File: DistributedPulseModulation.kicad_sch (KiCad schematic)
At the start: 59 parts, among them J1 Conn_02x12_Odd_Even, J2 Conn_01x01, U1 74LS251, U10 4053, U11 4053, U12 4053, U25 74LS85, U28 74LS85, U31 74LS85, U4 MCP23017_SP, U7 4053, U8 4040, U9 4040

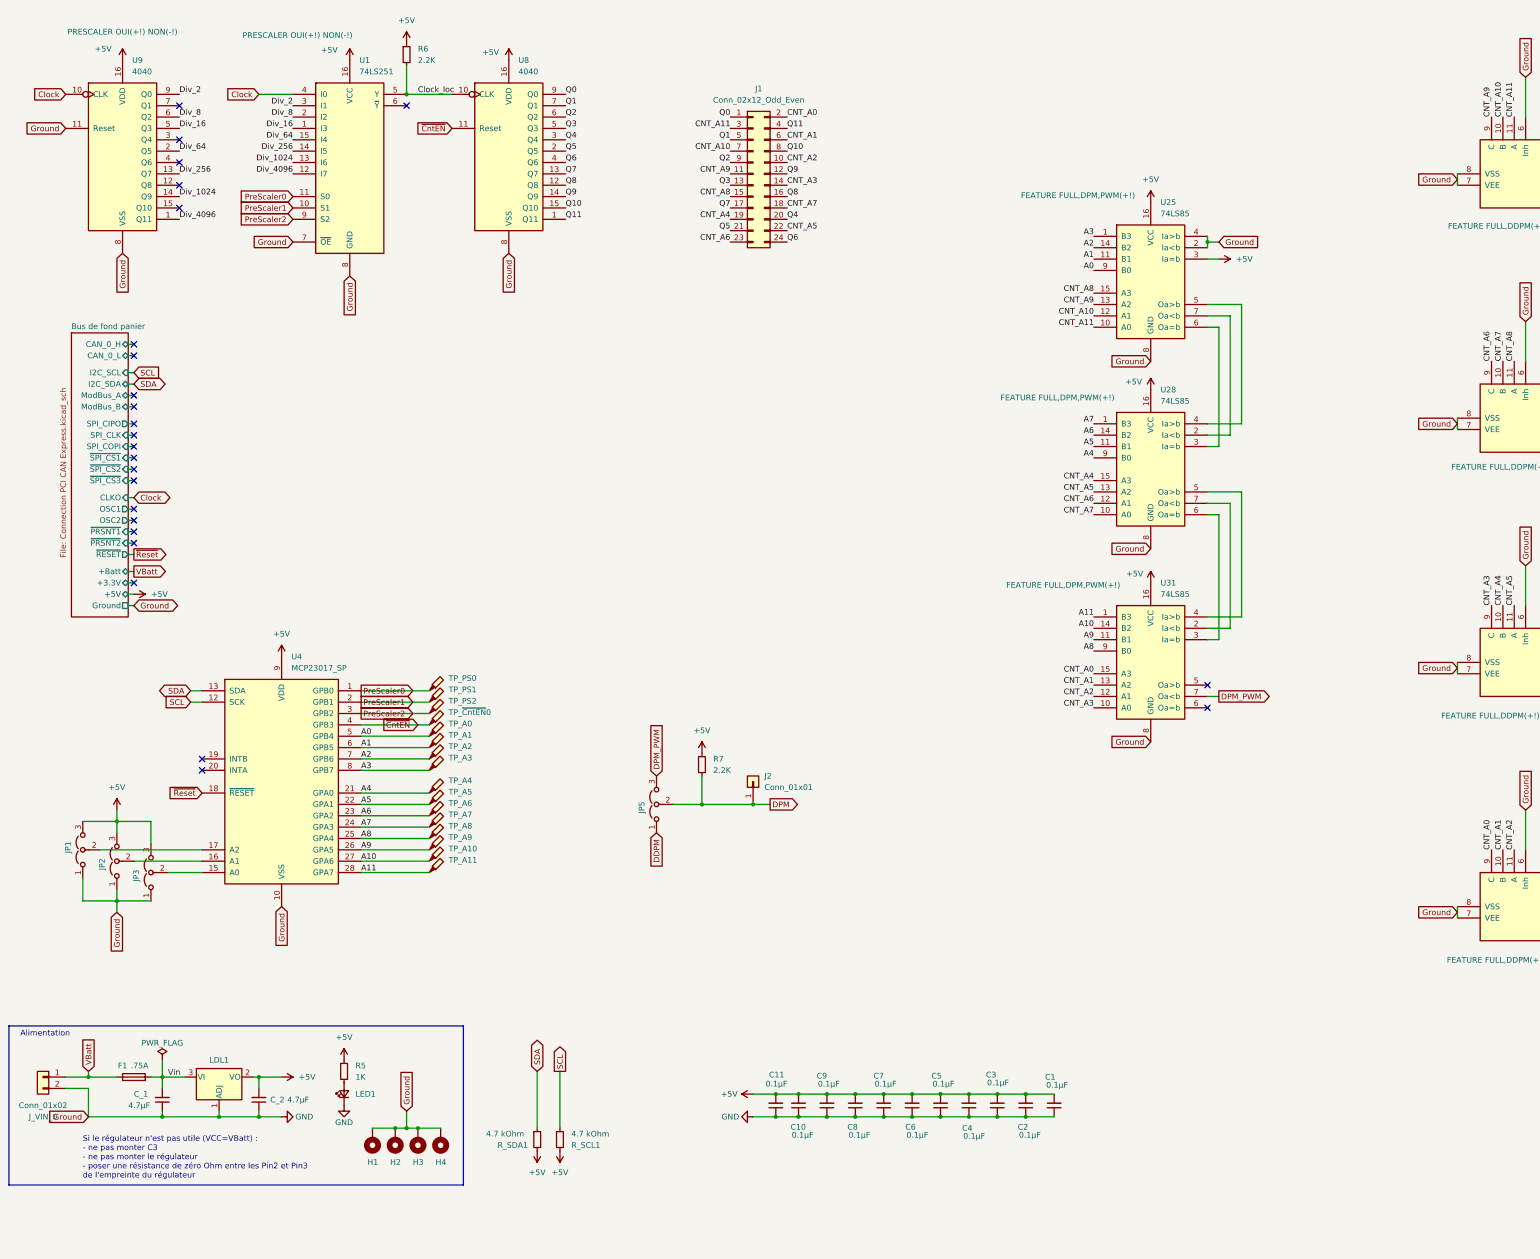
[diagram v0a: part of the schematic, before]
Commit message: [UPGRADE] : V2.1 in progress :-)
[DONE]
-> A jout de R7 (2.2K) en pull-up sur la sortie finale de la carte
-> A jout de R7 (2.2K) en pull-up sur la sortie clock locale
-> Bascule D sur sortie carte pour anti-rebond
-> retrait régulateur de tension
-> déplacement jumper d'adressage
-> ajout décodeur BCD vers 7 segment
-> ajout afficheur 7 segments sur l'addresse
-> détournement du "dot point" en tant que "power led"
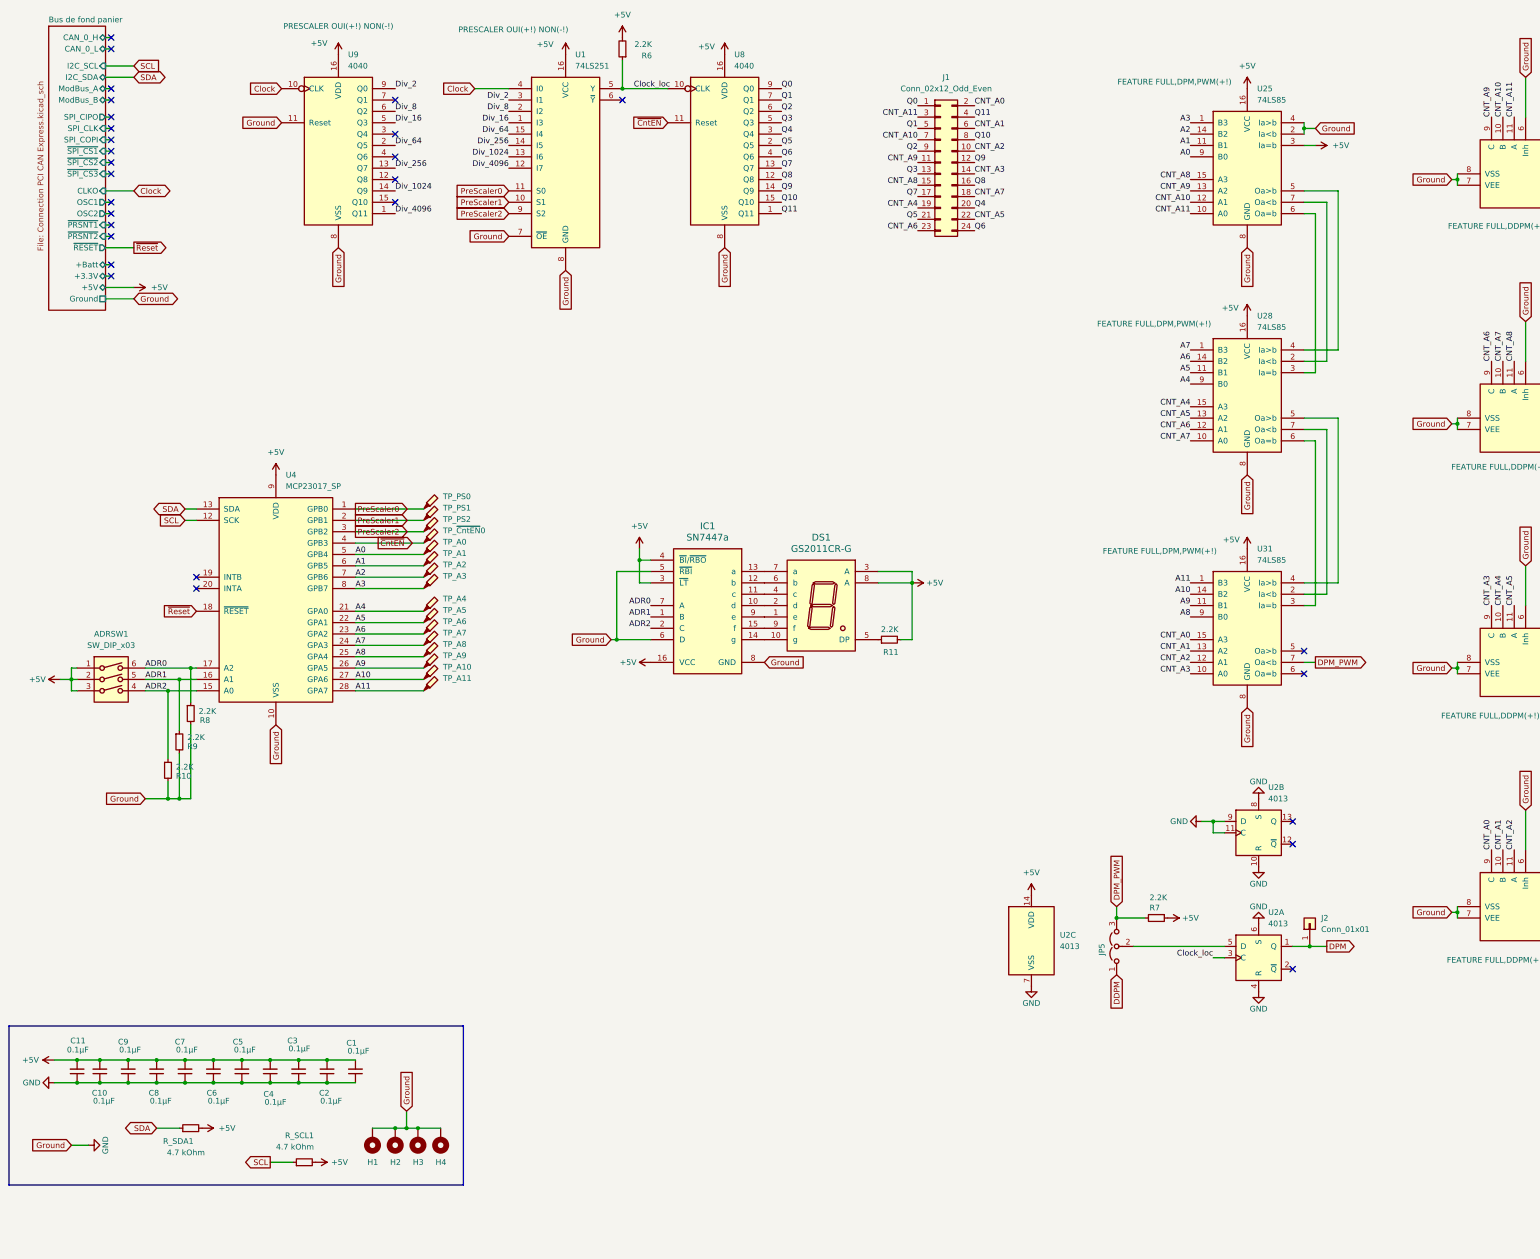
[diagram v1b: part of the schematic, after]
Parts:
- removed C_1, C_2: 4.7µF, Capacitor_SMD:C_1206_3216Metric_Pad1.33x1.80mm_HandSolder, symbol Device:C_Small
- removed F1: .75A, Fuse:Fuse_1206_3216Metric_Pad1.42x1.75mm_HandSolder, symbol Device:Fuse
- removed JP1, JP2, JP3: Jumper_3_Open, Connector_PinHeader_2.54mm:PinHeader_1x03_P2.54mm_Vertical, symbol Jumper:Jumper_3_Open
- removed J_VIN_0: Conn_01x02, TerminalBlock_TE-Connectivity:TerminalBlock_TE_282834-2_1x02_P2.54mm_Horizontal, symbol Connector_Generic:Conn_01x02
- removed LDL1: LDL1117, Package_TO_SOT_SMD:SOT-223-3_TabPin2, symbol Regulator_Linear:LM317_SOT-223
- removed LED1: LED, LED_SMD:LED_1206_3216Metric_Pad1.42x1.75mm_HandSolder, symbol Device:LED_Small
- removed R5: 1K, Resistor_SMD:R_1206_3216Metric_Pad1.30x1.75mm_HandSolder, symbol Device:R_Small
- added ADRSW1: SW_DIP_x03, Button_Switch_SMD:SW_DIP_SPSTx03_Slide_6.7x9.18mm_W8.61mm_P2.54mm_LowProfile, symbol Switch:SW_DIP_x03
- added DS1: GS2011CR-G, Display_7Segment:KCSC02-105, symbol LEDs & Displays:7-Segment Red Display CA Type1
- added IC1: SN7447a, Package_SO:SOIC-16_3.9x9.9mm_P1.27mm, symbol Standard Logic:7447
- added R10, R11, R8, R9: 2.2K, Resistor_THT:R_Axial_DIN0207_L6.3mm_D2.5mm_P2.54mm_Vertical, symbol Device:R_Small
- added U2: 4013, Package_DIP:DIP-14_W7.62mm_Socket, symbol 4xxx:4013
- R6, R7: footprint Resistor_SMD:R_1206_3216Metric_Pad1.30x1.75mm_HandSolder -> Resistor_THT:R_Axial_DIN0207_L6.3mm_D2.5mm_P2.54mm_Vertical
- R_SCL1, R_SDA1: footprint Resistor_THT:R_Axial_DIN0207_L6.3mm_D2.5mm_P10.16mm_Horizontal -> Resistor_THT:R_Axial_DIN0207_L6.3mm_D2.5mm_P2.54mm_Vertical
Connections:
- net +5V: now also R6.2, ADRSW1.1, ADRSW1.2, ADRSW1.3, DS1.3 (A), DS1.8 (A), IC1.16 (VCC), IC1.3 (~{LT}), IC1.4 (~{BI}/~{RBO}), R11.2, U2.14 (VDD); no longer R6.1
- net Clock_loc: now also R6.1, U2.3 (C); no longer R6.2
- net DPM: now also U2.1 (Q); no longer JP5.2 (C), R7.2
- net DPM_PWM: now also R7.2
- net GND: now also IC1.5 (~{RBI}), IC1.6 (D), IC1.8 (GND), R10.2, R8.2, R9.2, U2.10 (R), U2.11 (C), U2.4 (R), U2.6 (S), U2.7 (VSS), U2.8 (S), U2.9 (D)
- net ADR0: now reaches U4.17 (A2)
- net ADR0: now also ADRSW1.6, IC1.7 (A), R8.1
- net ADR2: now reaches U4.15 (A0)
- net ADR2: now also ADRSW1.4, IC1.2 (C), R10.1
- net ADR1: now reaches U4.16 (A1)
- net ADR1: now also ADRSW1.5, IC1.1 (B), R9.1
- new net: JP5.2 (C), U2.5 (D)
- new net: DS1.5 (DP), R11.1
- new net: DS1.1 (e), IC1.9 (e)
- new net: DS1.10 (g), IC1.14 (g)
- new net: DS1.2 (d), IC1.10 (d)
- new net: DS1.4 (c), IC1.11 (c)
- new net: DS1.6 (b), IC1.12 (b)
- new net: DS1.7 (a), IC1.13 (a)
- new net: DS1.9 (f), IC1.15 (f)
- no-connect marks 25 -> 29
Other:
- note removed: "Alimentation"
- note removed: "Si le régulateur n'est pas utile (VCC=VBatt) : - ne pas monter C3 - ne pas monter le régulateur - poser une résistance de zéro Ohm entre les Pin2 et Pin3 de l'empreinte du régulateur"
- moved on the sheet: C1, C10, C11, C2, C3, C4, C5, C6, C7, C8, C9, J1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

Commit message: [update] : choix aficheurs et conv ; bug pin A1 ; condo ; doc pdf
- choix du 7-segment en common anode
- choix de decodeur DCBN vers 7-segments
- bug routage pin A1 sur V2.0 de la carte
- condo découplage sur D-latch
- condo découplage sur DVBN->7-segments
- ajout doc pdf work-in-progress
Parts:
- removed DS1: GS2011CR-G, Display_7Segment:KCSC02-105, symbol LEDs & Displays:7-Segment Red Display CA Type1
- added C12, C13: 0.1µF, Capacitor_THT:C_Disc_D5.0mm_W2.5mm_P5.00mm, symbol Device:C_Small
- added DS1: GS2011AR-G, Display_7Segment:KCSC02-105, symbol Display_Character:KCSA02-105
- IC1: value SN7447a -> SN74LS247
- R11: value 2.2K -> 330
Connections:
- net +5V: now also C12.2, C13.2, DS1.3 (CA), DS1.8 (CA); no longer R11.2
- net GND: now also R11.1, C12.1, C13.1; no longer IC1.8 (GND)
- net at IC1.9 (e): now also DS1.1 (E)
- net at IC1.14 (g): now also DS1.10 (G)
- net at IC1.10 (d): now also DS1.2 (D)
- net at IC1.11 (c): now also DS1.4 (C)
- net at IC1.12 (b): now also DS1.6 (B)
- net at IC1.13 (a): now also DS1.7 (A)
- net at IC1.15 (f): now also DS1.9 (F)
- new net: DS1.5 (DP), IC1.8 (GND), R11.2
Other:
- moved on the sheet: ADRSW1, C1, C10, C11, C2, C3, C4, C5, C6, C7, C8, C9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

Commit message: [UPDATE] : KiVar ; doc pdf
- adding KiVar command to some new parts
- pdf datasheet list up-to-date
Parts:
- ADRSW1: KiLib_Generator (none) -> button_switch/DIP
- C12, C13: KiLib_Generator (none) -> capacitor/THT/other; Var FEATURE FULL,DDPM(+!) -> (none)
- IC1: KiLib_Generator (none) -> package/gullwing
- R10, R11, R8, R9, R_SCL1, R_SDA1: KiLib_Generator (none) -> resistor/THT
- R6: KiLib_Generator (none) -> resistor/THT; Var (none) -> PRESCALER OUI(+!) NON(-!)
- R7: KiLib_Generator (none) -> resistor/THT; Var (none) -> FEATURE FULL,DPM,PWM(+!)
- U2: KiLib_Generator (none) -> package/DIP/legacy
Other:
- note added: "CMOS I2C IOexp : MCP23017 E/SP CMOS CPT : CD74HCT4040E TTL MUX : 74LS251N TTL COMP : SN74LS85N CMOS 3SPDT : CD74HCT4053E CMOS D-latch : CD4013B Without Prescaler => NOK (due to TTL to CMOS link) ----------------- DPM/PWM CMOS(IOexp)->CMOS(CPT)->TTL(COMP)->CMOS(D-latch) DDPM CMOS(IOexp)->CMOS(CPT)->CMOS(SPDT)->CMOS(D-latch) With Prescaler => NOK (due to TTL to CMOS link) -------------- DPM/PWM CMO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"
- note removed: "CMOS I2C IOexp : MCP23017 E/SP CMOS CPT : CD74HCT4040E TTL MUX : 74LS251N TTL COMP : SN74LS85N CMOS 3SPDT : CD74HCT4053E Without Prescaler => OK ----------------- DPM/PWM CMOS(IOexp)->CMOS(CPT)->TTL(COMP) DDPM CMOS(IOexp)->CMOS(CPT)->CMOS(SPDT) With Prescaler => NOK -------------- DPM/PWM CMOS(IOexp)->CMOS(CPT)->TTL(MUX)->CMOS(CPT)->TTL(COMP) DDPM CMOS(IOexp)->CMOS(CPT)->TTL(MUX)->CMOS(CPT)->CMOS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"
- moved on the sheet: C1, C10, C11, C12, C13, C2, C3, C4, C5, C6, C7, C8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

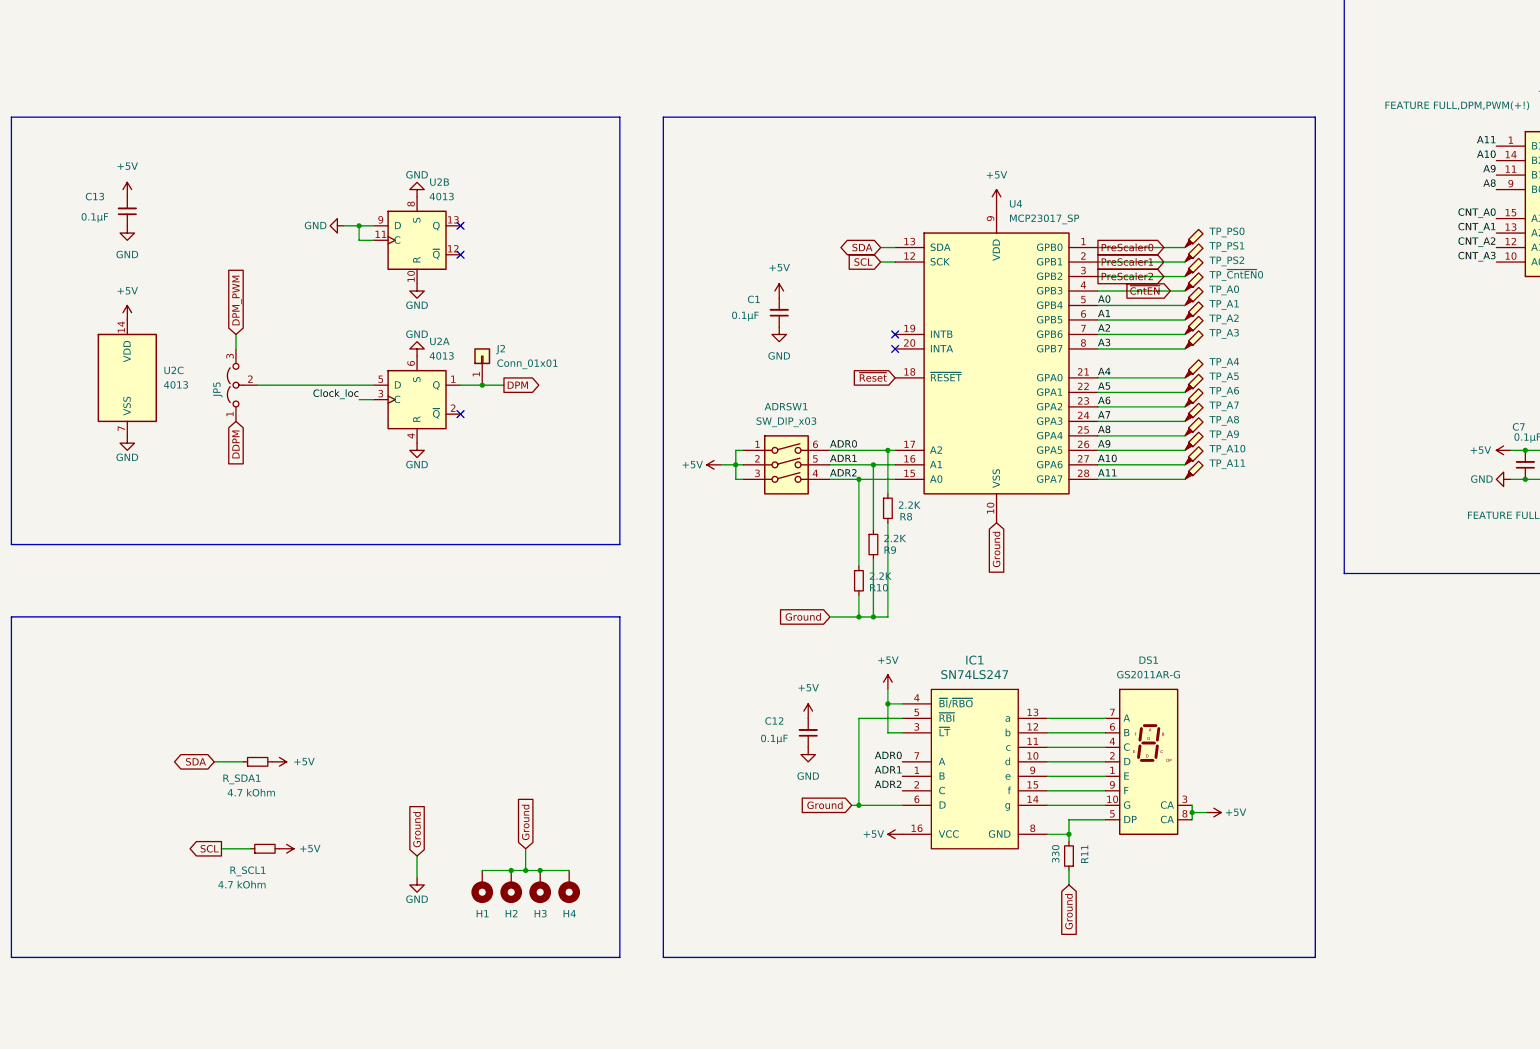
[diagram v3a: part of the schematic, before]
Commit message: [update] : missing resistors on the 7 segmznts display
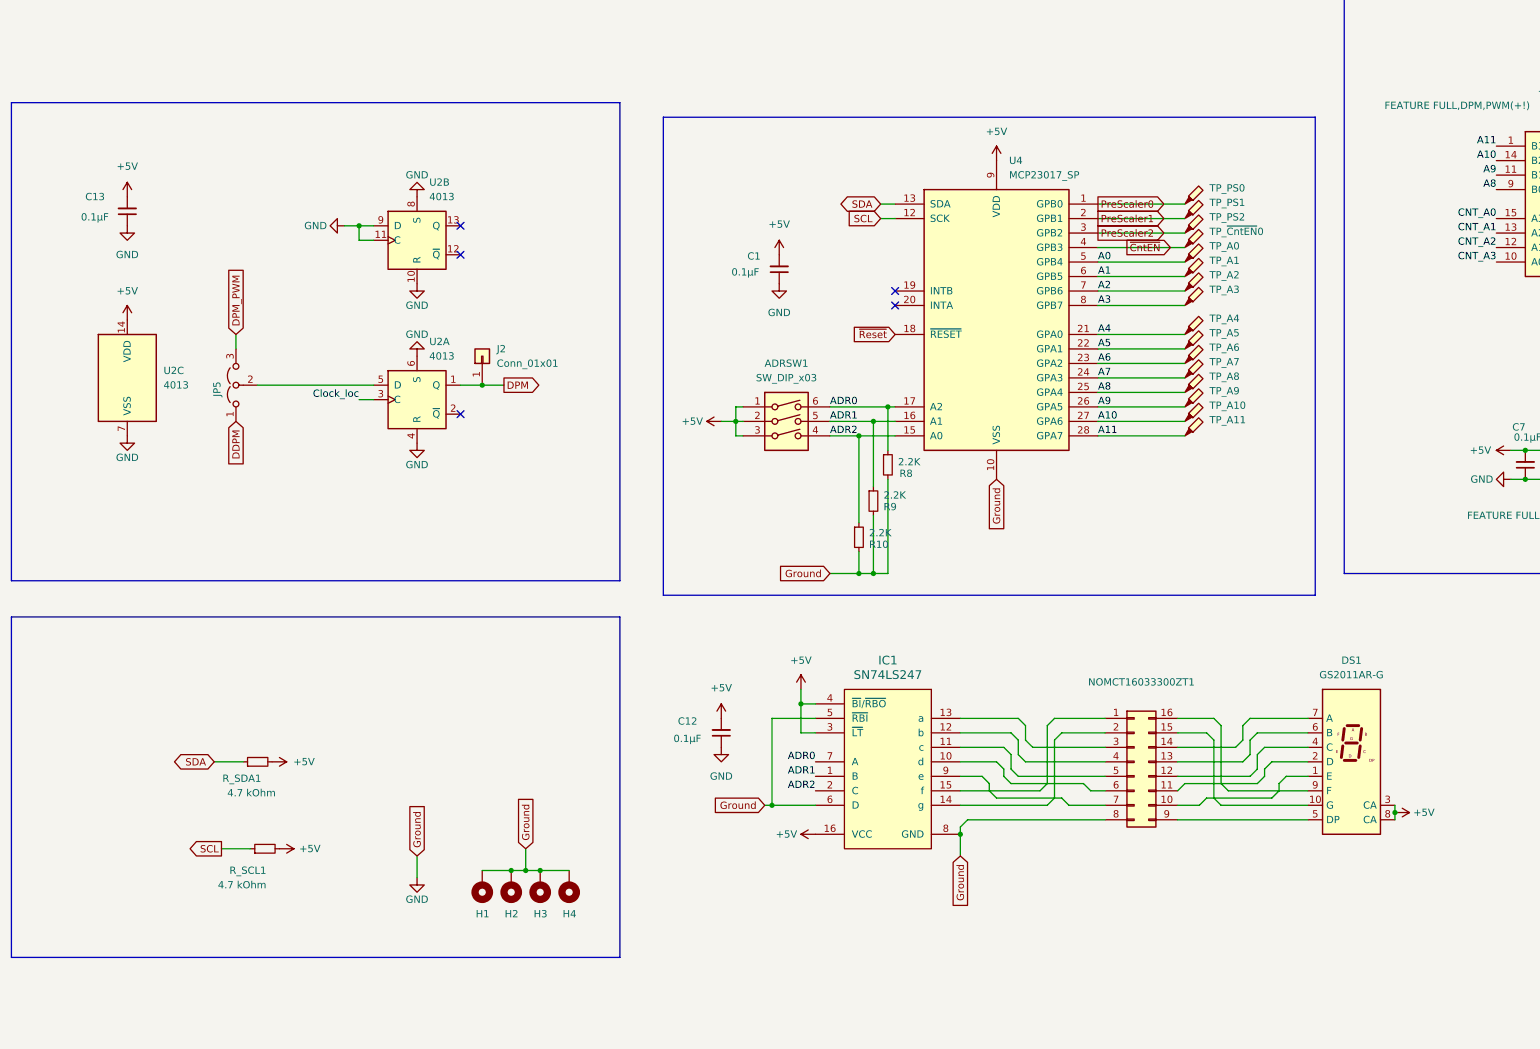
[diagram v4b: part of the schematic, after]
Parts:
- removed R11: 330, Resistor_THT:R_Axial_DIN0207_L6.3mm_D2.5mm_P2.54mm_Vertical, symbol Device:R_Small
- added NOMCT16033300ZT1: Conn_02x08_Counter_Clockwise, Package_SO:JEITA_SOIC-16_3.9x9.9mm_P1.27mm, symbol Connector_Generic:Conn_02x08_Counter_Clockwise
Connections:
- net GND: now also IC1.8 (GND), NOMCT16033300ZT1.8 (Pin_8)
- net at DS1.1 (E): now also NOMCT16033300ZT1.10 (Pin_10); no longer IC1.9 (e)
- net at DS1.10 (G): now also NOMCT16033300ZT1.15 (Pin_15); no longer IC1.14 (g)
- net at DS1.2 (D): now also NOMCT16033300ZT1.11 (Pin_11); no longer IC1.10 (d)
- net at DS1.4 (C): now also NOMCT16033300ZT1.12 (Pin_12); no longer IC1.11 (c)
- net at DS1.5 (DP): now also NOMCT16033300ZT1.9 (Pin_9); no longer IC1.8 (GND)
- net at DS1.6 (B): now also NOMCT16033300ZT1.13 (Pin_13); no longer IC1.12 (b)
- net at DS1.7 (A): now also NOMCT16033300ZT1.14 (Pin_14); no longer IC1.13 (a)
- net at DS1.9 (F): now also NOMCT16033300ZT1.16 (Pin_16); no longer IC1.15 (f)
- new net: IC1.10 (d), NOMCT16033300ZT1.6 (Pin_6)
- new net: IC1.11 (c), NOMCT16033300ZT1.5 (Pin_5)
- new net: IC1.12 (b), NOMCT16033300ZT1.4 (Pin_4)
- new net: IC1.13 (a), NOMCT16033300ZT1.3 (Pin_3)
- new net: IC1.14 (g), NOMCT16033300ZT1.2 (Pin_2)
- new net: IC1.15 (f), NOMCT16033300ZT1.1 (Pin_1)
- new net: IC1.9 (e), NOMCT16033300ZT1.7 (Pin_7)
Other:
- moved on the sheet: ADRSW1, C1, C12, DS1, IC1, R10, R8, R9, TP_A0, TP_A1, TP_A10, TP_A11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
